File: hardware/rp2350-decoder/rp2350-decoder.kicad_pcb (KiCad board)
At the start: 6 copper layers, 19.9 x 8.8 mm, 68 parts, among them J1 SWDIO, J2 SWCLK, J3 5052702412, Q1 DMN2991UDA-7B, Q2 DMN2991UDA-7B, Q3 NST847BPDP6T5G, Q4 NST847BPDP6T5G, Q5 DMN2991UDA-7B, Q6 DMN2991UDA-7B, Q7 DMN2991UDA-7B, Q8 DMN2991UDA-7B, SW1 BOOT, U1 NCS2220AMUT1G, U2 AP63203WU, U3 W25Q128JVPIQ, U4 RP2350A, U5 MAX98357AEWL+T, U6 MD9927, Y1 ABM8-272-T3

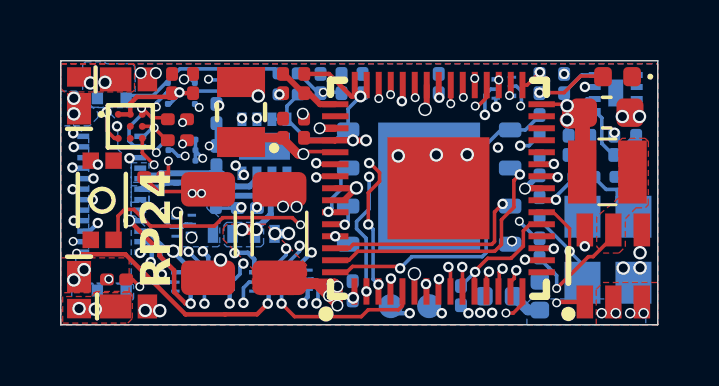
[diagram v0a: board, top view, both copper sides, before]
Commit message: fix: un-swap capacitor shutdown circuit inputs
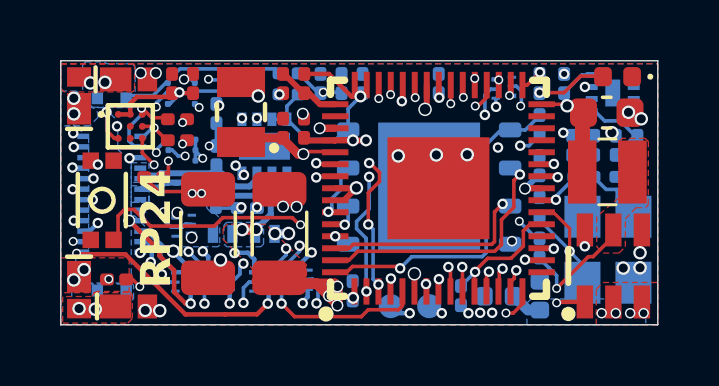
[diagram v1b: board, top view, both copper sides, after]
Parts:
- moved R3 1.57 mm to (118.5, 102.6)
- moved R4 1.57 mm to (119.2, 102.6)
- moved R1 1.40 mm to (117.0, 102.6)
- moved R2 1.40 mm to (117.8, 102.6)
- moved U1 0.10 mm to (118.4, 100.8)
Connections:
- R1 pad 2: /COMP_P -> /COMP_N
- R2 pad 1: /COMP_P -> /COMP_N
- R3 pad 2: /COMP_N -> /COMP_P
- R4 pad 1: /COMP_N -> /COMP_P
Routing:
- net +3.3V: track 30.3 -> 27.7 mm
- net VDC: track 13.3 -> 11.5 mm

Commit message: feat: zener diodes to detect both waves and cutouts
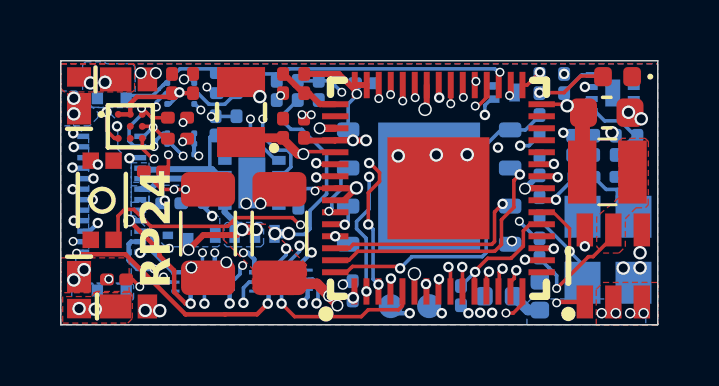
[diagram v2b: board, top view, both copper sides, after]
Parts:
- removed C12: 100nF, rp2350-decoder:C_0201_0603Metric
- removed C21: 470pF, rp2350-decoder:C_0201_0603Metric
- removed Q1: DMN2991UDA-7B, rp2350-decoder:X2-DFN0806-6_L0.8-W0.6_X2-DFN0806-6
- added D10: GDZ3V3LP3-7, rp2350-decoder:D_0201_0603Metric, B.Cu at (108.6, 100.7)
- added D8: GDZ3V3LP3-7, rp2350-decoder:D_0201_0603Metric, B.Cu at (107.2, 100.7)
- added Q9: AP1606, rp2350-decoder:DFN-3L_L1.0-W0.6-P0.65-BR, B.Cu at (114.8, 100.8)
- Q2: value DMN2991UDA-7B -> AP1606; footprint rp2350-decoder:X2-DFN0806-6_L0.8-W0.6_X2-DFN0806-6 -> rp2350-decoder:DFN-3L_L1.0-W0.6-P0.65-BR
- R8: value 2.2K -> 6.8K
- moved C20 3.47 mm to (107.9, 104.3), turned to -90 degrees
- moved R8 3.16 mm to (105.5, 100.2), turned to 0 degrees
- moved R17 2.53 mm to (103.7, 104.5), turned to 0 degrees
- moved U6 1.29 mm to (106.4, 103.8), turned to 90 degrees
- moved R18 0.99 mm to (105.2, 101.9)
- moved R12 0.82 mm to (105.5, 100.8)
- moved R19 0.79 mm to (105.9, 101.9), turned to 90 degrees
- moved R7 0.64 mm to (107.9, 100.7), turned to -90 degrees
- moved Q2 0.57 mm to (103.9, 105.8), turned to 180 degrees
- moved R16 0.44 mm to (104.8, 104.1)
- moved Q3 0.21 mm to (104.0, 102.5)
- moved R11 0.19 mm to (103.1, 103.4)
- moved C3 0.07 mm to (110.1, 100.5), turned to 0 degrees
- moved D6 0.07 mm to (105.5, 105.5)
- moved R10 0.05 mm to (103.9, 101.6)
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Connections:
- Q2 pad 1: /CAP+ -> /CAP_ENABLE
- Q2 pad 2: /CAP_ENABLE -> /CAP+
- R7 pad 1: Net-(Q1A-G1) -> /VDC_ZENER
- R7 pad 2: /TRACK_LEFT -> VDC
- R8 pad 1: GND -> /TRACK_LEFT
- R8 pad 2: Net-(Q1A-G1) -> /DCC_TTL
- U4 pad 41: GND -> /VDC_ZENER
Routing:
- net Net-(Q1A-G1): track 10.2 -> 0.00 mm, vias 2 -> 0
- net /DCC_TTL: track 0.01 -> 9.25 mm
- net VDC: track 11.5 -> 17.8 mm
- net /VDC_ZENER: track 0.00 -> 4.73 mm, vias 0 -> 2
- net /CAP_VDC: track 12.0 -> 9.35 mm, vias 11 -> 9
- net /GPIO25: track 8.02 -> 10.5 mm
- net /TRACK_LEFT: track 5.49 -> 3.38 mm
- net /MOTOR_A: track 5.08 -> 3.13 mm
- net /GPIO26: track 7.45 -> 9.21 mm
- net /CAP_ENABLE: track 16.3 -> 14.7 mm
- net /AUX1 (VDC): track 3.90 -> 5.44 mm
- net +3.3V: track 27.7 -> 26.3 mm, vias 14 -> 15
- net /ADC_EMF_A: track 7.64 -> 9.09 mm
- net GND: track 4.57 -> 3.33 mm, vias 34 -> 31
- net /AUX12: track 16.2 -> 15.3 mm
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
